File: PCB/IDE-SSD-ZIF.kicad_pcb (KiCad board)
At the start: 4 copper layers, 49 x 68.5 mm, 84 parts, among them J1 Conn_01x40_Female, U1 SM2236, U2 LP38691SD-1.8, U3 FlashBGA152, U4 FlashBGA152, U5 FlashBGA152, U6 FlashBGA152

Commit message: Changed 1.8V reg
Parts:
- added G***: LOGO, cust:doslab_logo, B.Cu at (148.2, 116.2)
- added REF**: OSHW-Symbol_8.9x8mm_SilkScreen, Symbol:OSHW-Symbol_8.9x8mm_SilkScreen, B.Cu at (119.2, 116.8)
- U2: value LP38691SD-1.8 -> TLV75518PDRV; footprint Package_SON:WSON-6-1EP_3x3mm_P0.95mm -> Package_SON:WSON-6-1EP_2x2mm_P0.65mm_EP1x1.6mm
- moved U2 1.27 mm to (117.8, 63.8), turned to 180 degrees
- turned C12 to 0 degrees
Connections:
- J1 pad 41: (no net) -> GND
- J1 pad 42: (no net) -> GND
- U2 pad 1: Net-(C12-Pad1) -> +VCCFQ
- U2 pad 2: GND -> unconnected-(U2-Pad2)
- U2 pad 3: unconnected-(U2-Pad3) -> GND
- U2 pad 4: +VCCFQ -> Net-(C12-Pad1)
- U2 pad 5: +VCCFQ -> unconnected-(U2-Pad5)
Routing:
- net Net-(C12-Pad1): track 9.39 -> 6.84 mm
- net +3V3: track 102.0 -> 102.2 mm, vias 62 -> 61
- net GND: vias 153 -> 152

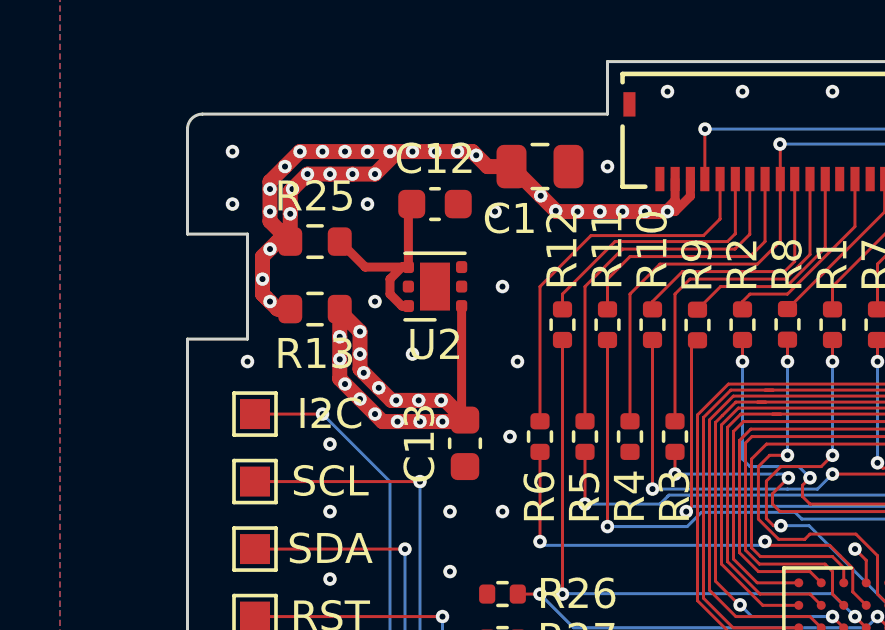
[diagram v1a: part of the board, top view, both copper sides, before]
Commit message: Fixed regulator footprint
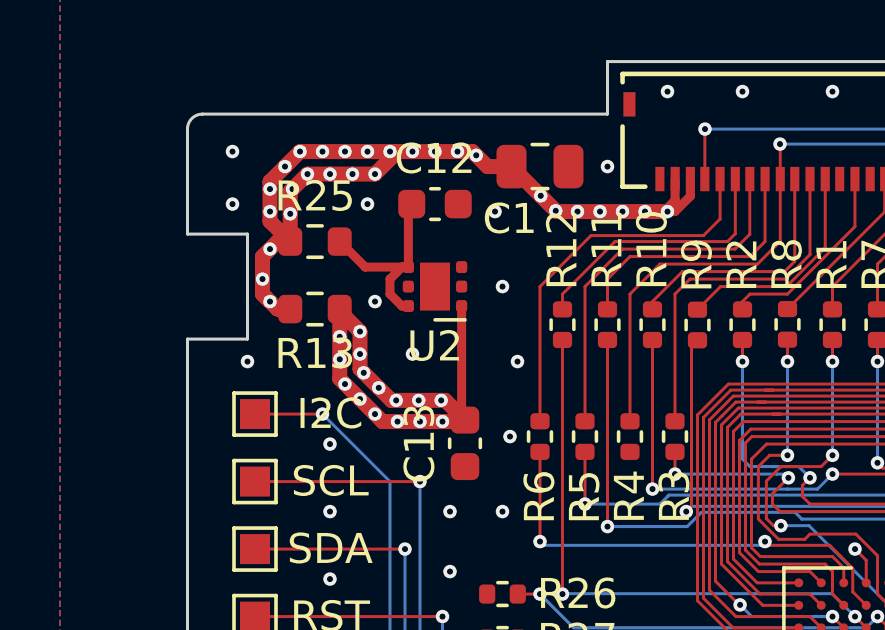
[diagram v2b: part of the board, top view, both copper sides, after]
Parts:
- U2: footprint Package_SON:WSON-6-1EP_2x2mm_P0.65mm_EP1x1.6mm -> cust:WSON-6-1EP_2x2mm_P0.65mm_EP1x1.6mm
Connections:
- J1 pad 41: GND -> (no net)
- J1 pad 42: GND -> (no net)
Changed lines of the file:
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@@
     (pad "40" smd rect (at -9.7536 -1.4986 270) (size 0.8128 0.3048) (layers "F.Cu" "F.Paste" "F.Mask")
       (net 35 "unconnected-(J1-Pad40)") (pinfunction "Pin_40") (pintype "passive"))
-    (pad "41" smd rect (at -10.7696 -3.9878) (size 0.4064 0.8128) (layers "F.Cu" "F.Paste" "F.Mask")
-      (net 4 "GND"))
-    (pad "42" smd rect (at 10.7696 -3.9878) (size 0.4064 0.8128) (layers "F.Cu" "F.Paste" "F.Mask")
-      (net 4 "GND"))
+    (pad "41" smd rect (at -10.7696 -3.9878) (size 0.4064 0.8128) (layers "F.Cu" "F.Paste" "F.Mask"))
+    (pad "42" smd rect (at 10.7696 -3.9878) (size 0.4064 0.8128) (layers "F.Cu" "F.Paste" "F.Mask"))
   )
   (footprint "Resistor_SMD:R_0402_1005Metric" (layer "F.Cu")
@@
     )
   )
-  (footprint "Package_SON:WSON-6-1EP_2x2mm_P0.65mm_EP1x1.6mm" (layer "F.Cu")
+  (footprint "cust:WSON-6-1EP_2x2mm_P0.65mm_EP1x1.6mm" (layer "F.Cu")
     (at 117.75 63.75 180)
     (descr "WSON, 6 Pin (http://www.ti.com/lit/ds/symlink/tps61040.pdf#page=35), generated with kicad-footprint-generator ipc_noLead_generator.py")
@@
     (property "Sheetname" "")
     (attr smd)
-    (fp_text reference "U2" (at 0 -1.95) (layer "F.SilkS")
+    (fp_text reference "U2" (at 0 -2 180) (layer "F.SilkS")
       (effects (font (size 1 1) (thickness 0.15)))
     )
-    (fp_text value "TLV75518PDRV" (at 0 1.95) (layer "F.Fab")
+    (fp_text value "TLV75518PDRV" (at 0 1.95 180) (layer "F.Fab")
       (effects (font (size 1 1) (thickness 0.15)))
     )
-    (fp_text user "${REFERENCE}" (at 0 0) (layer "F.Fab")
+    (fp_text user "${REFERENCE}" (at 0 0 180) (layer "F.Fab")
       (effects (font (size 0.5 0.5) (thickness 0.08)))
     )
-    (fp_line (start -1 1.11) (end 1 1.11) (layer "F.SilkS") (width 0.12))
-    (fp_line (start 0 -1.11) (end 1 -1.11) (layer "F.SilkS") (width 0.12))
+    (fp_line (start -1 -1.11) (end 0 -1.11) (layer "F.SilkS") (width 0.12))
+    (fp_line (start 1.32 -1.25) (end -1.32 -1.25) (layer "F.CrtYd") (width 0.05))
+    (fp_line (start 1.32 1.25) (end 1.32 -1.25) (layer "F.CrtYd") (width 0.05))
     (fp_line (start -1.32 -1.25) (end -1.32 1.25) (layer "F.CrtYd") (width 0.05))
     (fp_line (start -1.32 1.25) (end 1.32 1.25) (layer "F.CrtYd") (width 0.05))
-    (fp_line (start 1.32 1.25) (end 1.32 -1.25) (layer "F.CrtYd") (width 0.05))
-    (fp_line (start 1.32 -1.25) (end -1.32 -1.25) (layer "F.CrtYd") (width 0.05))
-    (fp_line (start -0.5 -1) (end 1 -1) (layer "F.Fab") (width 0.1))
     (fp_line (start 1 -1) (end 1 1) (layer "F.Fab") (width 0.1))
-    (fp_line (start 1 1) (end -1 1) (layer "F.Fab") (width 0.1))
     (fp_line (start -1 -0.5) (end -0.5 -1) (layer "F.Fab") (width 0.1))
+    (fp_line (start -0.5 -1) (end 1 -1) (layer "F.Fab") (width 0.1))
+    (fp_line (start 1 1) (end -1 1) (layer "F.Fab") (width 0.1))
     (fp_line (start -1 1) (end -1 -0.5) (layer "F.Fab") (width 0.1))
-    (pad "" smd roundrect (at 0 -0.4 180) (size 0.81 0.64) (layers "F.Paste") (roundrect_rratio 0.25))
     (pad "" smd roundrect (at 0 0.4 180) (size 0.81 0.64) (layers "F.Paste") (roundrect_rratio 0.25))
+    (pad "" smd roundrect (at 0 -0.4 180) (size 0.81 0.64) (layers "F.Paste") (roundrect_rratio 0.25))
     (pad "1" smd roundrect (at -0.8875 -0.65 180) (size 0.375 0.4) (layers "F.Cu" "F.Paste" "F.Mask") (roundrect_rratio 0.25)
       (net 135 "+VCCFQ") (pinfunction "OUT") (pintype "power_out"))
